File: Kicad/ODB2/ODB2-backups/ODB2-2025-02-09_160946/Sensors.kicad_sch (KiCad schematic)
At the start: 16 parts, among them J4 RF2-04A-T-00-50-G, U5 L76L-M33, U6 ICM-20948, U7 MS580301BA01-00

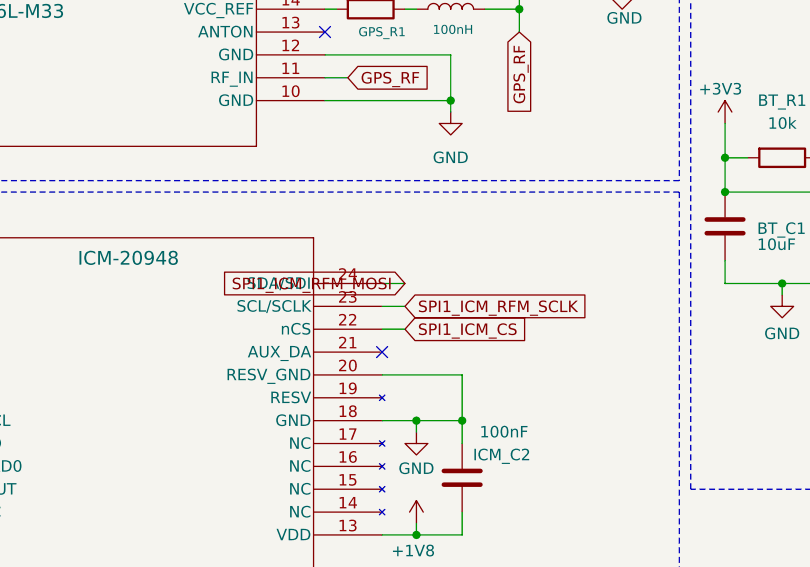
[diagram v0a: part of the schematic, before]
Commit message: Changed XNOR Gate and OP AMP to 1 chanel
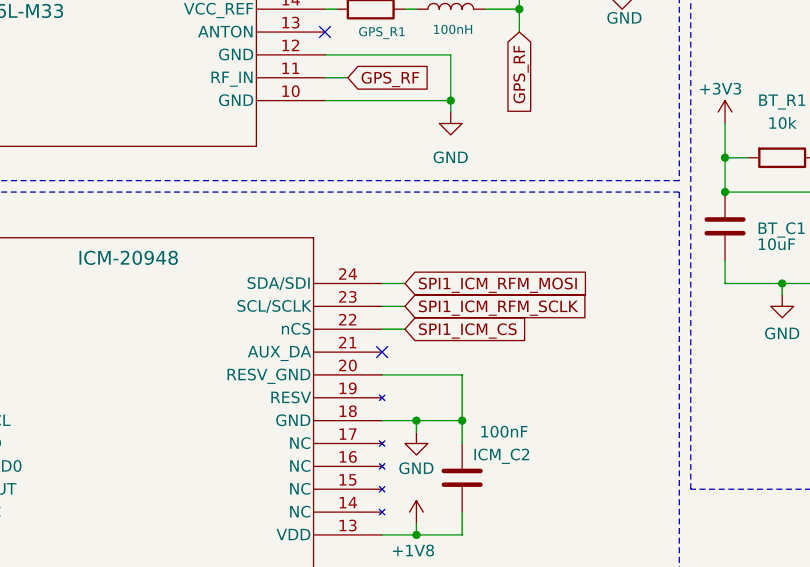
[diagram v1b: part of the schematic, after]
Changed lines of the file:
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@@
 	(global_label "SPI1_ICM_RFM_MOSI"
 		(shape input)
-		(at 114.3 74.93 180)
+		(at 114.3 74.93 0)
 		(fields_autoplaced yes)
 		(effects
@@
 				(size 1.27 1.27)
 			)
-			(justify right)
+			(justify left)
 		)
 		(property "Intersheetrefs" "${INTERSHEET_REFS}"
-			(at 92.3858 74.93 0)
+			(at 136.2142 74.93 0)
 			(effects
 				(font
 					(size 1.27 1.27)
 				)
-				(justify right)
+				(justify left)
 				(hide yes)
 			)
